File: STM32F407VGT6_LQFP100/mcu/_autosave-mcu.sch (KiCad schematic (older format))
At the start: 13 parts, among them SW1 SW_Push, U1 STM32F407VGT6

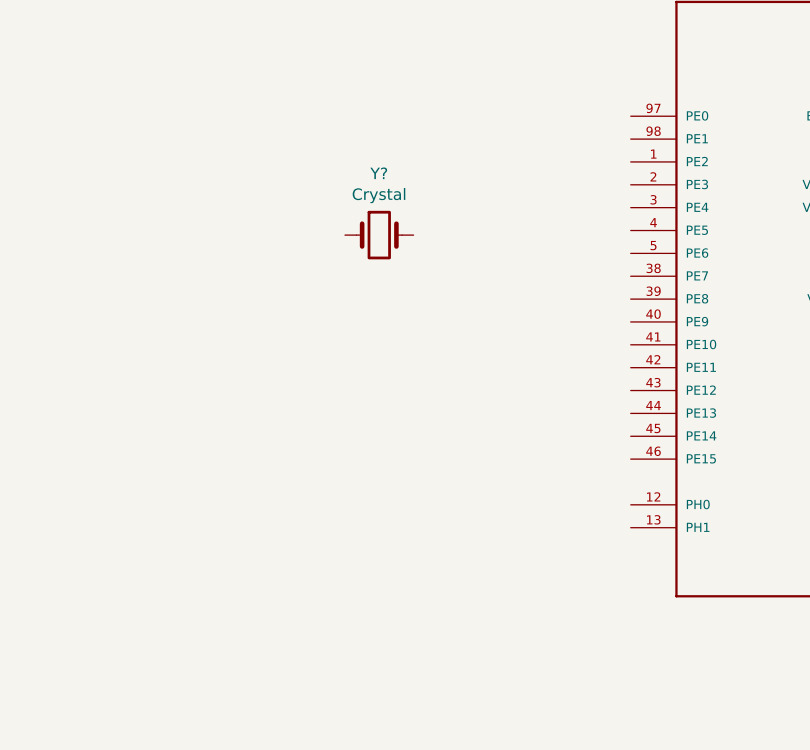
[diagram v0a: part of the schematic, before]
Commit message: add oscillator
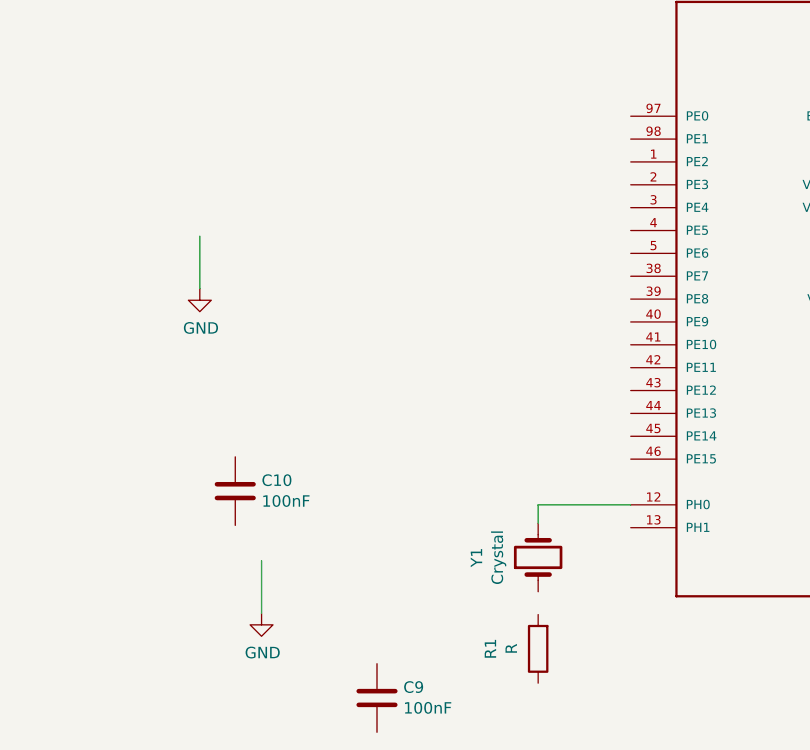
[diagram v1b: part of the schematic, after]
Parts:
- added C10, C9: 100nF, symbol Device:C
- added R1: R, symbol Device:R
- gave numbers to parts that had none: 1
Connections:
- wire segments 52 -> 56
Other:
- moved on the sheet: Y1
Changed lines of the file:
@@
 EESchema Schematic File Version 4
+LIBS:mcu-cache
 EELAYER 29 0
 EELAYER END
@@
 	9660 4495 9660 4630
 $Comp
-L Device:Crystal Y?
+L Device:Crystal Y1
 U 1 1 5F5AB575
-P 6470 3325
-F 0 "Y?" H 6470 3593 50  0000 C CNN
-F 1 "Crystal" H 6470 3502 50  0000 C CNN
-F 2 "" H 6470 3325 50  0001 C CNN
-F 3 "~" H 6470 3325 50  0001 C CNN
-	1    6470 3325
-	1    0    0    -1
+P 7165 4735
+F 0 "Y1" H 7165 5003 50  0000 C CNN
+F 1 "Crystal" H 7165 4912 50  0000 C CNN
+F 2 "" H 7165 4735 50  0001 C CNN
+F 3 "~" H 7165 4735 50  0001 C CNN
+	1    7165 4735
+	0    -1   -1   0
 $EndComp
 Wire Wire Line
@@
 Wire Wire Line
 	1900 4975 2280 4975
+$Comp
+L Device:R R1
+U 1 1 5F56953D
+P 7165 5135
+F 0 "R1" V 7372 5135 50  0000 C CNN
+F 1 "R" V 7281 5135 50  0000 C CNN
+F 2 "" V 7095 5135 50  0001 C CNN
+F 3 "~" H 7165 5135 50  0001 C CNN
+	1    7165 5135
+	-1   0    0    1
+$EndComp
+Wire Wire Line
+	5955 4750 5955 4980
+$Comp
+L power:GND #PWR?
+U 1 1 5F56FC84
+P 5955 4980
+F 0 "#PWR?" H 5955 4730 50  0001 C CNN
+F 1 "GND" H 5960 4807 50  0000 C CNN
+F 2 "" H 5955 4980 50  0001 C CNN
+F 3 "" H 5955 4980 50  0001 C CNN
+	1    5955 4980
+	1    0    0    -1
+$EndComp
+Wire Wire Line
+	5685 3330 5685 3560
+$Comp
+L power:GND #PWR?
+U 1 1 5F571FF5
+P 5685 3560
+F 0 "#PWR?" H 5685 3310 50  0001 C CNN
+F 1 "GND" H 5690 3387 50  0000 C CNN
+F 2 "" H 5685 3560 50  0001 C CNN
+F 3 "" H 5685 3560 50  0001 C CNN
+	1    5685 3560
+	1    0    0    -1
+$EndComp
+$Comp
+L Device:C C9
+U 1 1 5F57F44D
+P 6460 5350
+F 0 "C9" H 6345 5304 50  0000 R CNN
+F 1 "100nF" H 6345 5395 50  0000 R CNN
+F 2 "" H 6498 5200 50  0001 C CNN
+F 3 "~" H 6460 5350 50  0001 C CNN
+	1    6460 5350
+	-1   0    0    1
+$EndComp
+$Comp
+L Device:C C10
+U 1 1 5F5834F5
+P 5840 4445
+F 0 "C10" H 5725 4399 50  0000 R CNN
+F 1 "100nF" H 5725 4490 50  0000 R CNN
+F 2 "" H 5878 4295 50  0001 C CNN
+F 3 "~" H 5840 4445 50  0001 C CNN
+	1    5840 4445
+	-1   0    0    1
+$EndComp
+Wire Wire Line
+	7570 4505 7165 4505
+Wire Wire Line
+	7165 4505 7165 4585
 $EndSCHEMATC
